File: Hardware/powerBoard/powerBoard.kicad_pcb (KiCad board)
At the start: 2 copper layers, 61 x 50 mm, 45 parts, among them IC1 MT3608, IC2 TP4056, IC3 DW01A-G, J1 DATA, J2 PWR, J3 AUX, Q1 FS8205A, Q2 AO3401A, SW1 SW_SPST, U2 AMS1117-3.3

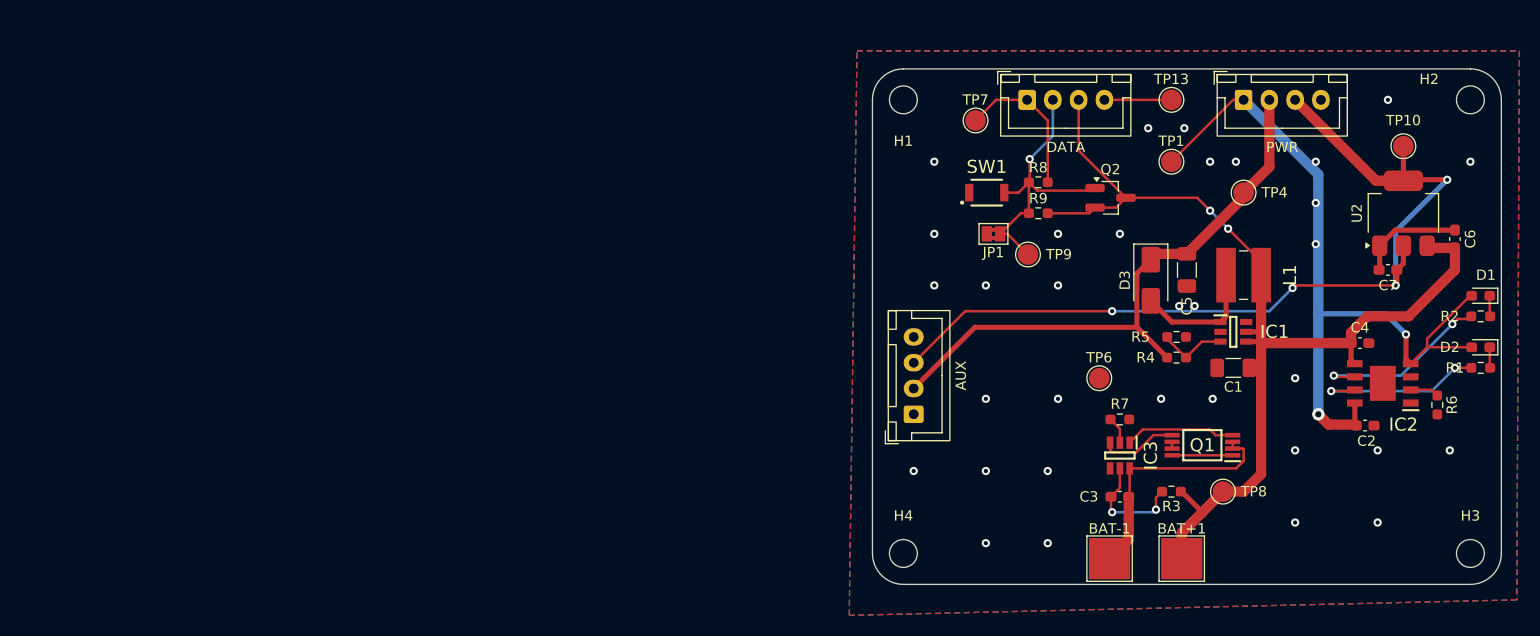
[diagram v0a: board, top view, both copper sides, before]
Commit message: refactor: relier le bouton poussoir à l'esp32
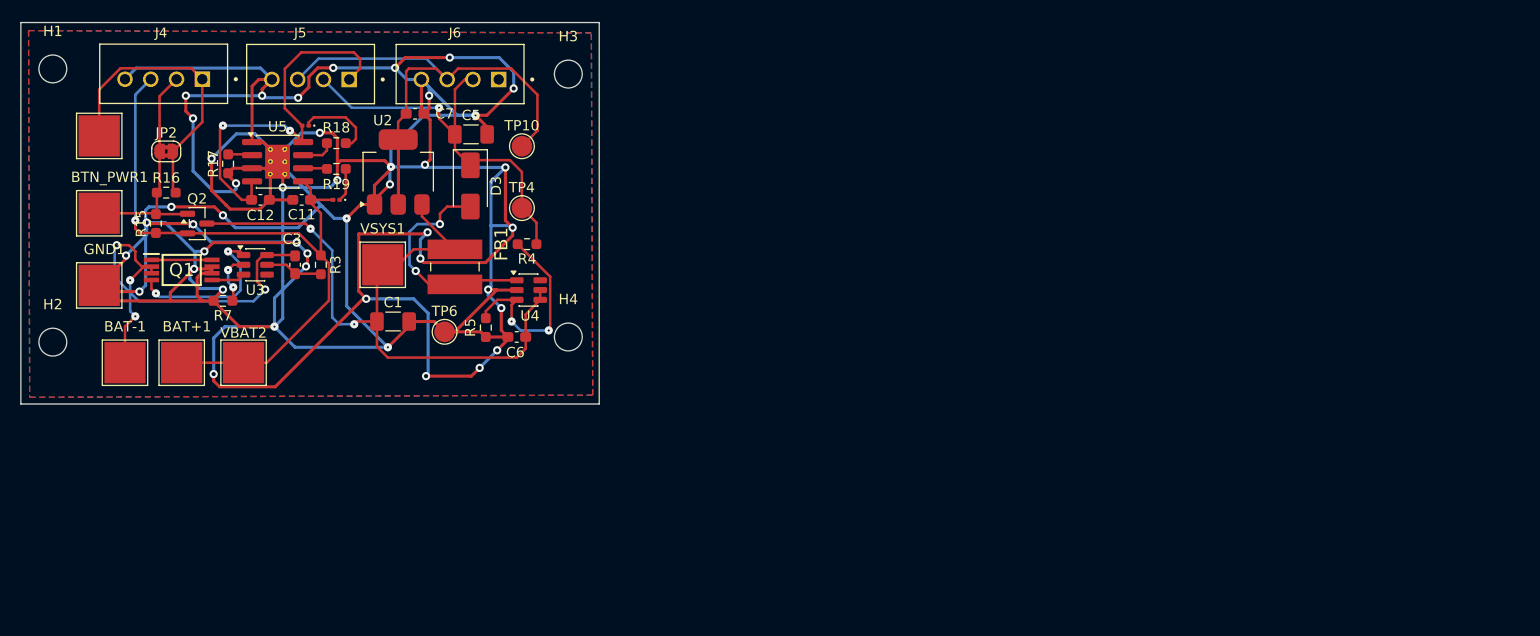
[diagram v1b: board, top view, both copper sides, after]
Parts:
- removed C2, C4: 10uF, Capacitor_SMD:C_0603_1608Metric_Pad1.08x0.95mm_HandSolder
- removed D1, D2: CHARGE, LED_SMD:LED_0603_1608Metric_Pad1.05x0.95mm_HandSolder
- removed IC1: MT3608, ChessLab:SOT95P280X145-6N
- removed IC2: TP4056, ChessLab:SOIC127P600X175-9N
- removed IC3: DW01A-G, ChessLab:SOT95P280X135-6N
- removed J1: DATA, Connector_JST:JST_XH_B4B-XH-A_1x04_P2.50mm_Vertical
- removed J2: PWR, Connector_JST:JST_XH_B4B-XH-A_1x04_P2.50mm_Vertical
- removed J3: AUX, Connector_JST:JST_XH_B4B-XH-A_1x04_P2.50mm_Vertical
- removed JP1: SolderJumper_2_Bridged, Jumper:SolderJumper-2_P1.3mm_Bridged2Bar_Pad1.0x1.5mm
- removed L1: CDRH4D28NP-2R2NC, ChessLab:CDRH4D28NP100NC
- removed R1, R2: 1k, Resistor_SMD:R_0603_1608Metric_Pad0.98x0.95mm_HandSolder
- removed R6: 1.1k, Resistor_SMD:R_0603_1608Metric_Pad0.98x0.95mm_HandSolder
- removed R8: 10k, Resistor_SMD:R_0603_1608Metric_Pad0.98x0.95mm_HandSolder
- removed R9: 100k, Resistor_SMD:R_0603_1608Metric_Pad0.98x0.95mm_HandSolder
- removed SW1: SW_SPST, ChessLab:B3U-1000P
- removed TP1: VBUS, TestPoint:TestPoint_Pad_D2.0mm
- removed TP13: GND, TestPoint:TestPoint_Pad_D2.0mm
- removed TP7: PWR_HOLD, TestPoint:TestPoint_Pad_D2.0mm
- removed TP8: VSYS, TestPoint:TestPoint_Pad_D2.0mm
- removed TP9: BTN_PWR, TestPoint:TestPoint_Pad_D2.0mm
- added BTN_PWR1: ~, TestPoint:TestPoint_Pad_4.0x4.0mm, F.Cu at (105.0, 64.0)
- added C11: 100µF, Capacitor_SMD:C_0603_1608Metric_Pad1.08x0.95mm_HandSolder, F.Cu at (124.6, 62.7)
- added C12: 100µF, Capacitor_SMD:C_0603_1608Metric_Pad1.08x0.95mm_HandSolder, F.Cu at (120.6, 62.7)
- added D4: LED, LED_SMD:LED_0201_0603Metric, F.Cu at (125.0, 55.5)
- added D5: LED, LED_SMD:LED_0201_0603Metric, F.Cu at (128.0, 62.7)
- added FB1: CDRH4D28NP-2R2NC, CDRH4D28_pretty:CDRH4D28NP100NC, F.Cu at (139.5, 69.2)
- added GND1: ~, TestPoint:TestPoint_Pad_4.0x4.0mm, F.Cu at (105.0, 71.0)
- added J4: DATA, pretty:JST_B4B-XH-A_LF__SN_, F.Cu at (111.2, 50.5)
- added J5: PWR, pretty:JST_B4B-XH-A_LF__SN_, F.Cu at (125.5, 50.5)
- added J6: AUX, pretty:JST_B4B-XH-A_LF__SN_, F.Cu at (140.0, 50.5)
- added JP2: SolderJumper_2_Bridged, Jumper:SolderJumper-2_P1.3mm_Bridged2Bar_RoundedPad1.0x1.5mm, F.Cu at (111.5, 58.0)
- added PWR_HOLD1: ~, TestPoint:TestPoint_Pad_4.0x4.0mm, F.Cu at (105.0, 56.5)
- added R15: 100k, Resistor_SMD:R_0603_1608Metric_Pad0.98x0.95mm_HandSolder, F.Cu at (110.5, 65.0)
- added R16: 10k, Resistor_SMD:R_0603_1608Metric_Pad0.98x0.95mm_HandSolder, F.Cu at (111.5, 62.0)
- added R17: 1.1k, Resistor_SMD:R_0603_1608Metric_Pad0.98x0.95mm_HandSolder, F.Cu at (117.5, 59.2)
- added R18: 1.1k, Resistor_SMD:R_0603_1608Metric_Pad0.98x0.95mm_HandSolder, F.Cu at (128.0, 57.2)
- added R19: 1.1k, Resistor_SMD:R_0603_1608Metric_Pad0.98x0.95mm_HandSolder, F.Cu at (128.0, 59.7)
- added U3: DW01A, Package_TO_SOT_SMD:SOT-23-6, F.Cu at (120.1, 69.0)
- added U4: MT3608, Package_TO_SOT_SMD:SOT-23-6, F.Cu at (146.6, 71.5)
- added U5: TP4056, Package_SO:SOIC-8-1EP_3.9x4.9mm_P1.27mm_EP2.41x3.3mm_ThermalVias, F.Cu at (122.3, 59.0)
- added VBAT2: ~, TestPoint:TestPoint_Pad_4.0x4.0mm, F.Cu at (119.0, 78.5)
- added VSYS1: ~, TestPoint:TestPoint_Pad_4.0x4.0mm, F.Cu at (132.5, 69.0)
- Q1: footprint ChessLab:SOP65P640X120-8N -> FS8205A_pretty:SOP65P640X120-8N
- Q2: value AO3401A -> AO3400A; footprint Package_TO_SOT_SMD:SOT-23_Handsoldering -> Package_TO_SOT_SMD:SOT-23
- moved H2 139.5 mm to (100.5, 76.5)
- moved Q1 100.4 mm to (113.0, 69.5), turned to 0 degrees
- moved H3 99.1 mm to (150.5, 50.5)
- moved BAT+1 98.8 mm to (113.0, 78.5)
- moved U2 97.6 mm to (134.0, 60.0)
- moved BAT-1 97.4 mm to (107.5, 78.5)
- moved C7 95.6 mm to (135.6, 54.4), turned to 0 degrees
- moved C6 91.5 mm to (145.5, 76.0), turned to 180 degrees
- moved Q2 88.6 mm to (114.5, 65.0)
- moved R7 87.8 mm to (117.0, 72.5), turned to 180 degrees
- moved TP10 85.5 mm to (146.0, 57.5)
- moved R3 85.4 mm to (126.5, 69.0), turned to -90 degrees
- moved C3 83.1 mm to (124.0, 69.0), turned to 90 degrees
- moved H1 82.6 mm to (100.5, 50.0)
- moved C1 81.6 mm to (133.5, 74.5), turned to 0 degrees
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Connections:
- C1 pad 1: /VBAT -> /VSYS
- C6 pad 1: /VBAT -> /VSYS
- Q2 pad 3: /VBAT -> /VSYS
- U2 pad 3: /VBAT -> /VSYS
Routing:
- net GND: track 17.5 -> 493.0 mm, vias 33 -> 44
- net /VSYS: track 0.00 -> 67.4 mm, vias 0 -> 2
- net /VBAT: track 110.4 -> 65.8 mm, vias 2 -> 1
- net /VBUS: track 75.2 -> 37.9 mm
- net +3V3: track 87.7 -> 56.1 mm, vias 4 -> 0
- net Net-(Q1-S1_1): track 23.8 -> 42.9 mm, vias 0 -> 4
- net +5V: track 57.4 -> 39.0 mm, vias 0 -> 1
- net Net-(IC2-~{STDBY}): track 17.8 -> 0.00 mm, vias 2 -> 0
- net Net-(IC2-~{CHRG}): track 16.9 -> 0.00 mm, vias 2 -> 0
- net /PWR_HOLD: track 14.7 -> 28.1 mm
- net Net-(U4-FB): track 6.74 -> 20.1 mm, vias 0 -> 2
- net Net-(D3-A): track 12.4 -> 22.1 mm, vias 0 -> 2
- net Net-(D4-K): track 0.00 -> 7.77 mm
- net /BTN_PWR: track 28.8 -> 22.5 mm, vias 1 -> 0
- net Net-(U3-VCC): track 11.0 -> 5.60 mm, vias 2 -> 0
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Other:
- board size 61 x 50 mm -> 56.1 x 37 mm

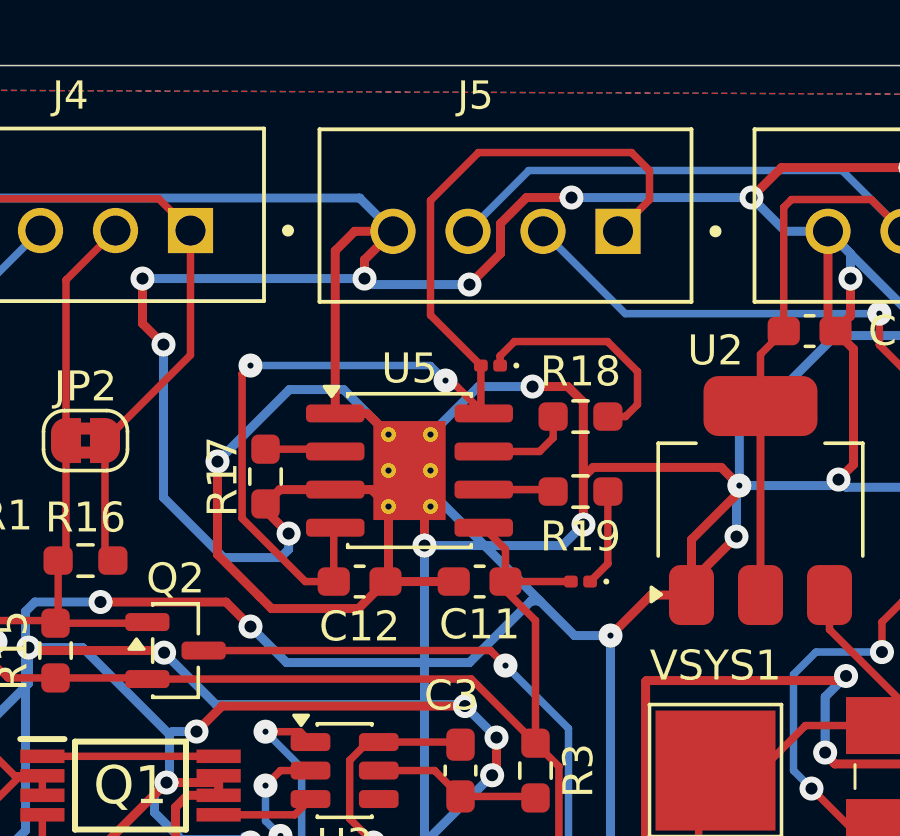
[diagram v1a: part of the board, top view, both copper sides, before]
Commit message: Diodes size fix
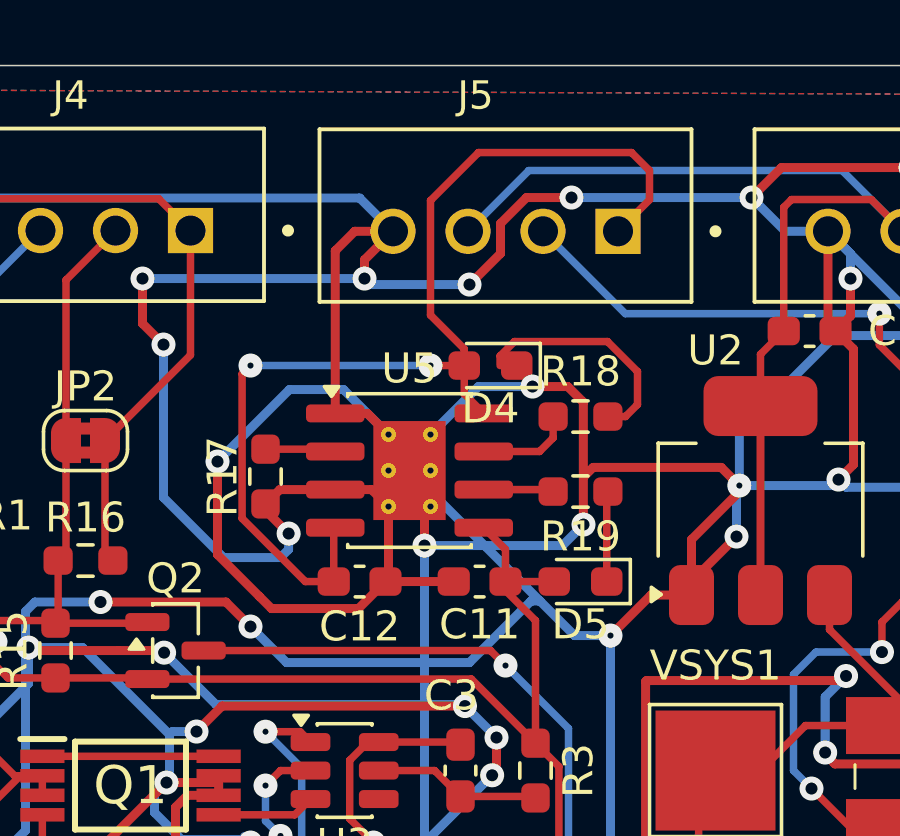
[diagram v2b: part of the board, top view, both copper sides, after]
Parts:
- D4, D5: footprint LED_SMD:LED_0201_0603Metric -> LED_SMD:LED_0603_1608Metric_Pad1.05x0.95mm_HandSolder
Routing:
- net /VBUS: track 37.9 -> 36.6 mm
- net /VBAT: track 65.8 -> 65.2 mm

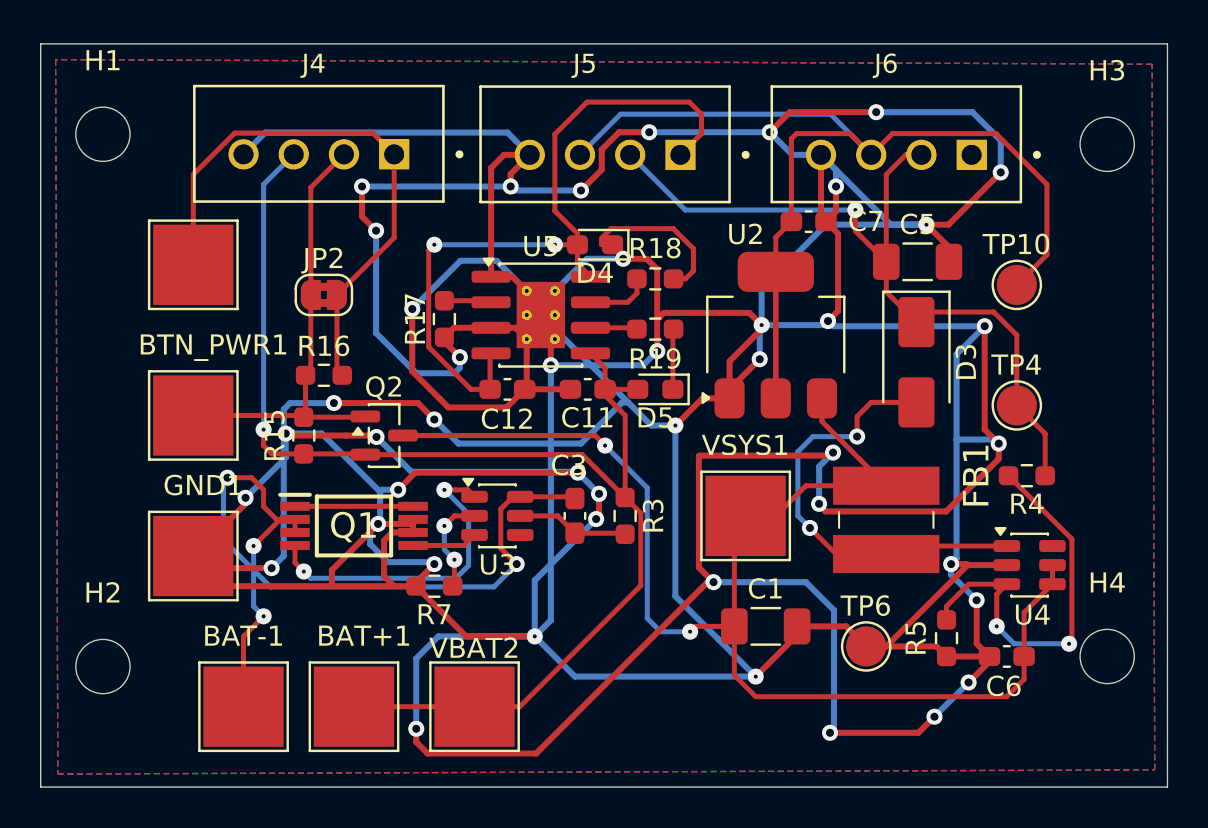
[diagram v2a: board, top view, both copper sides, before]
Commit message: ajout des vias et le nom sur la carte
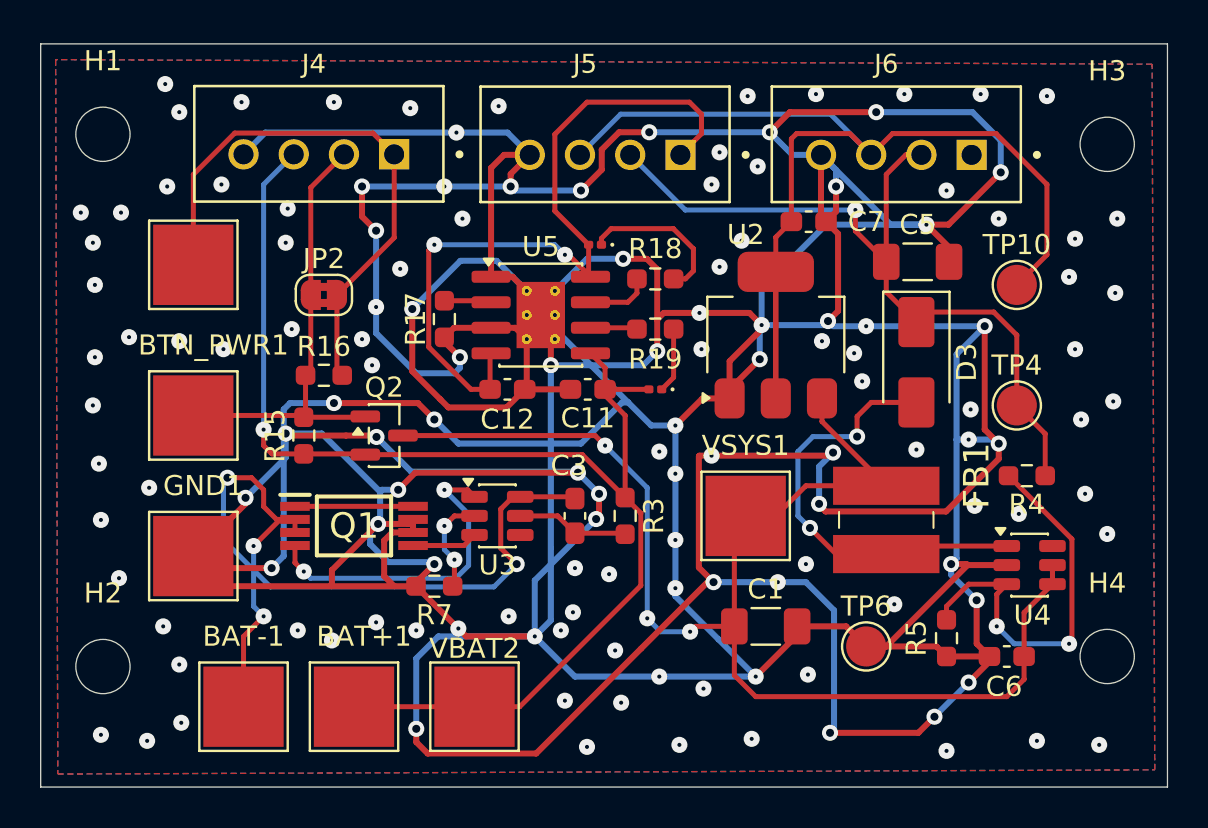
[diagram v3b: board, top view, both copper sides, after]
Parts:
- D4, D5: footprint LED_SMD:LED_0603_1608Metric_Pad1.05x0.95mm_HandSolder -> LED_SMD:LED_0201_0603Metric
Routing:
- net /VBUS: track 36.6 -> 37.9 mm
- net /VBAT: track 65.2 -> 65.8 mm
- net GND: vias 44 -> 142
- net /VSYS: vias 2 -> 3
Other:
- board text added: "CAMPUS FAB"
- board text added: "MAMADOU MOUCTAR BA ET ALEXANDRU CARP"
